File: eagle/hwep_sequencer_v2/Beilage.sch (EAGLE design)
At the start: 183 parts, among them X1 ESP32-AZDEL

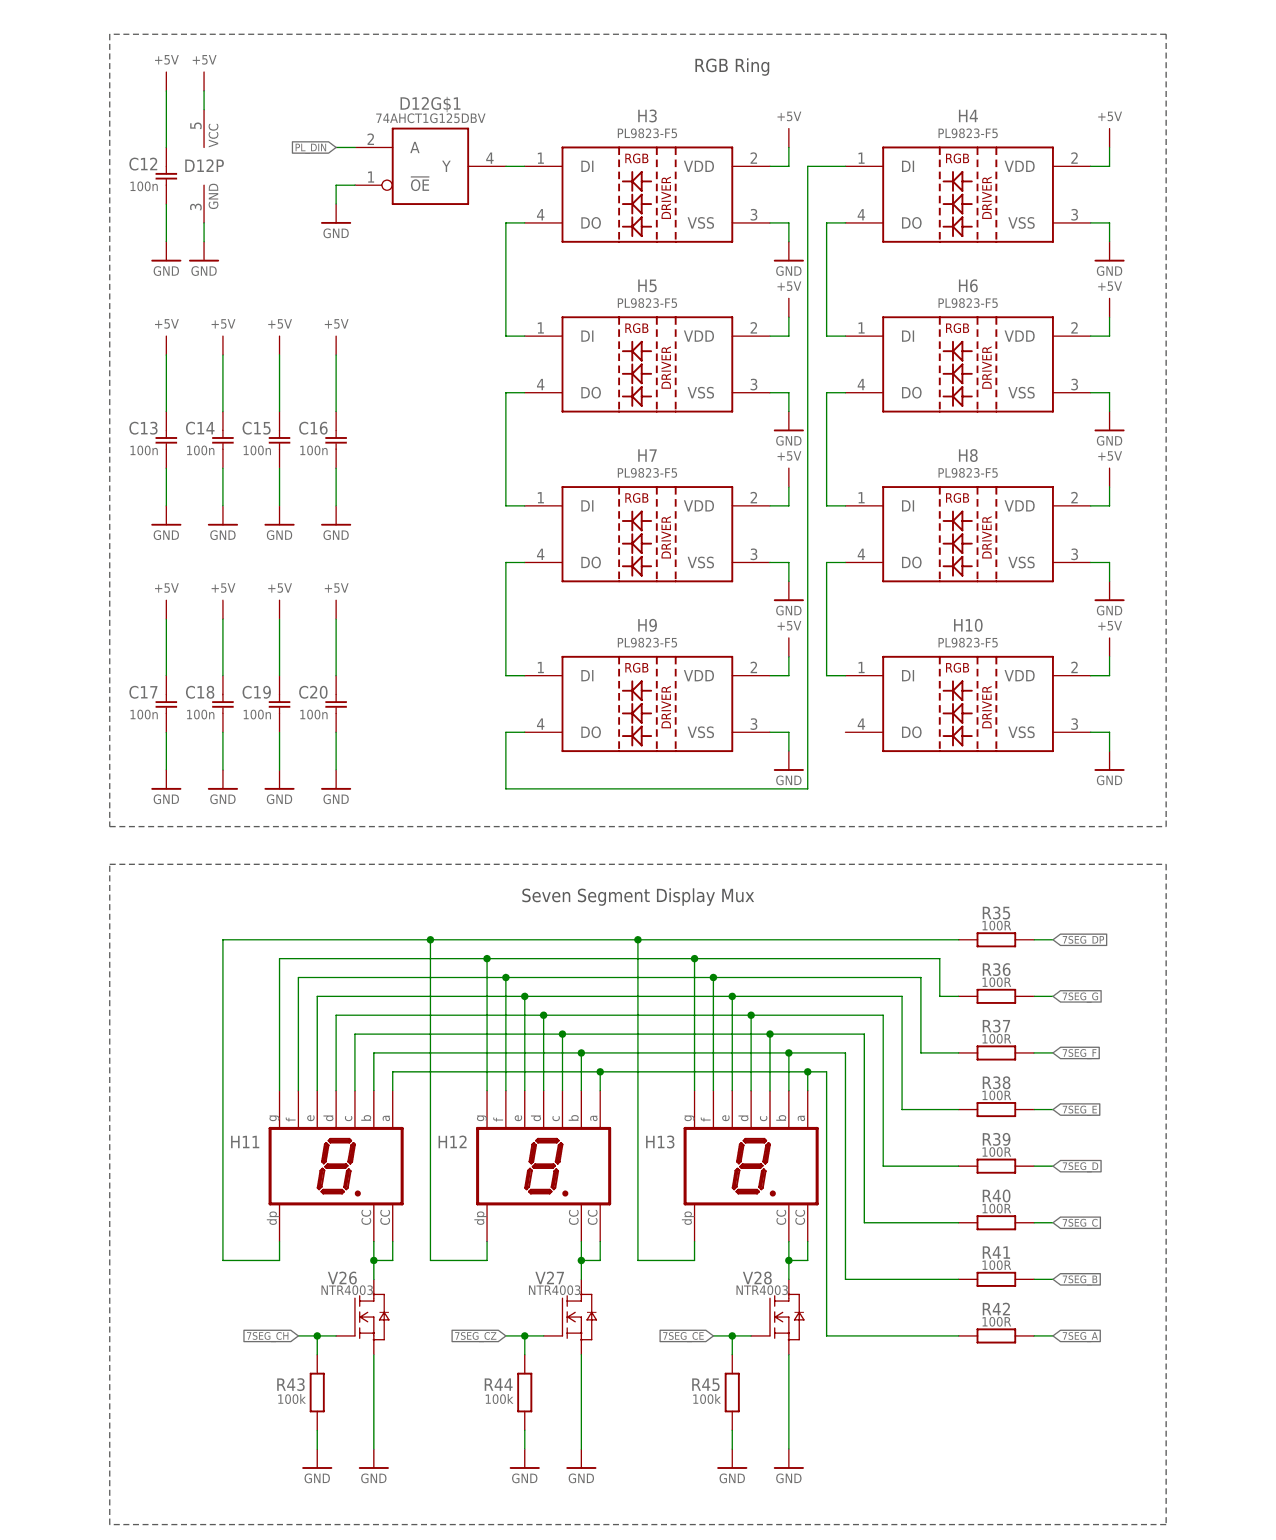
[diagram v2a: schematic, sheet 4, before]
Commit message: RGB Ring now in SMD
SMD RGB LEDS WS2812 used because of availability
PSU Buck Converter 12v to 5v still to be added to the schematic
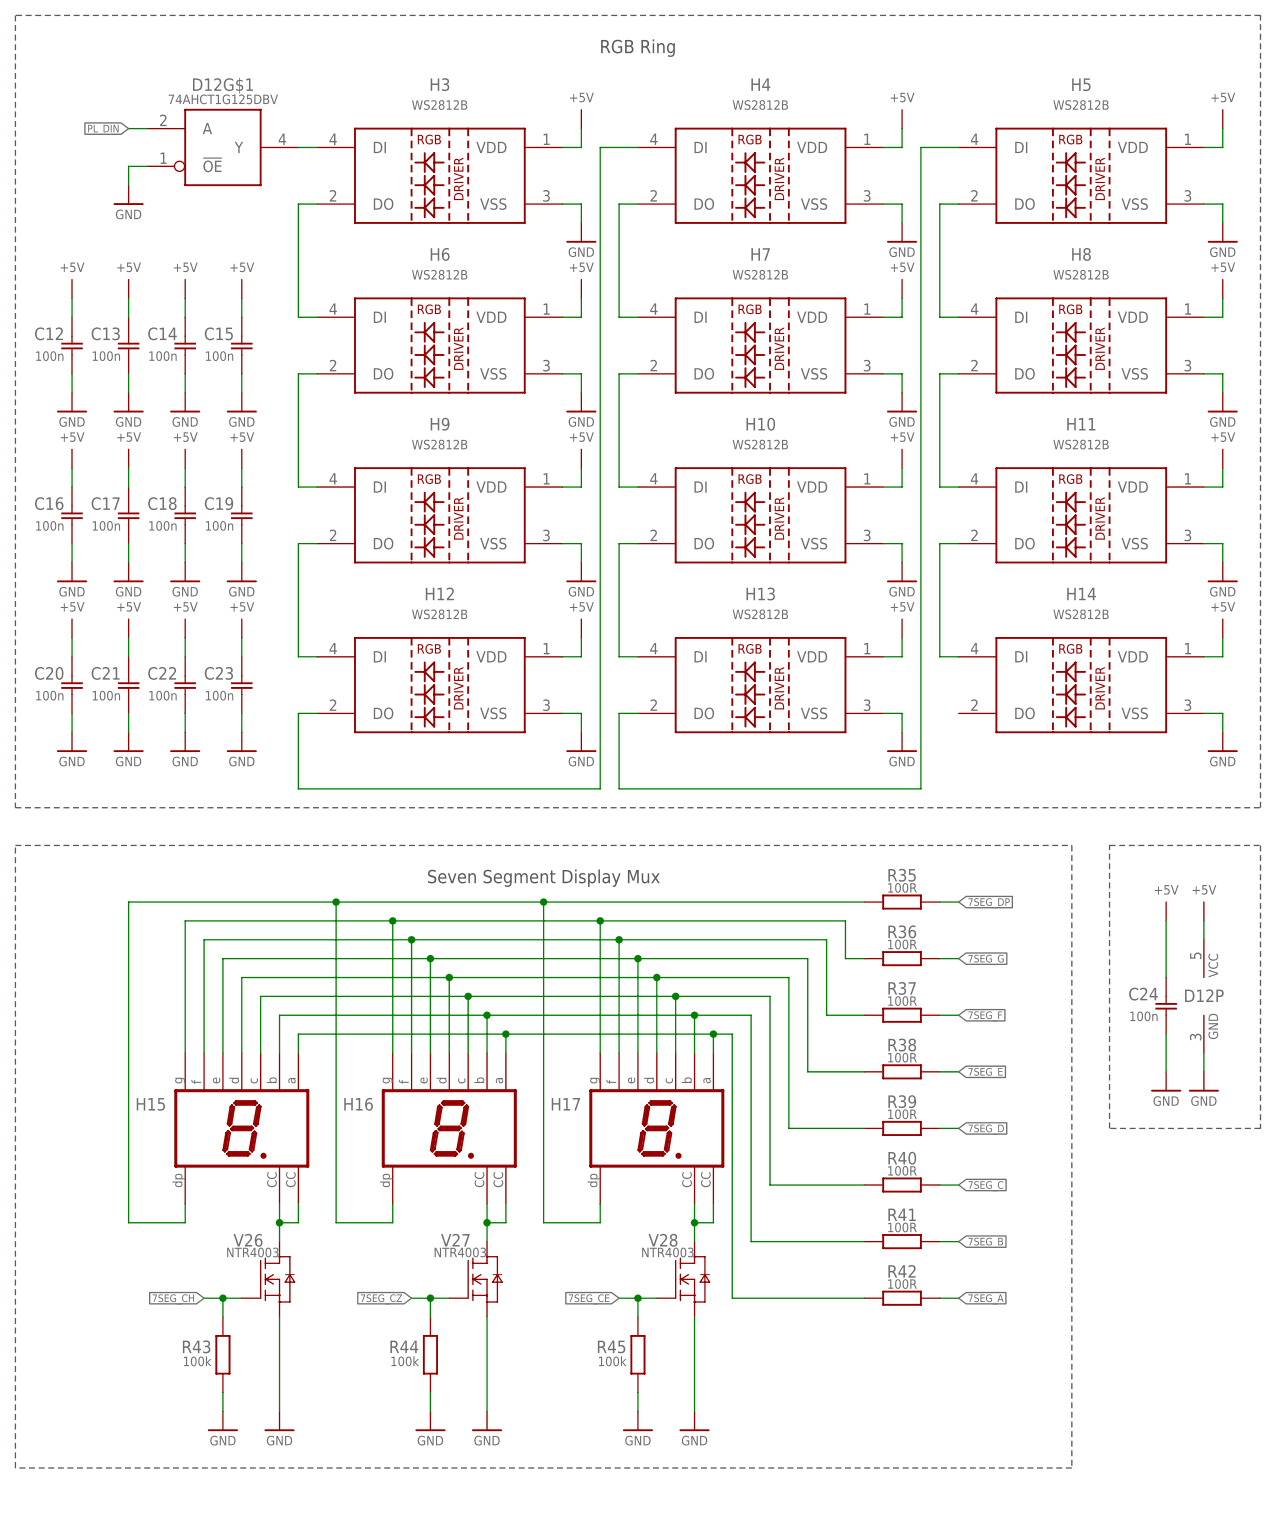
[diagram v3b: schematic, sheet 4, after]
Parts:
- added C29, C30: 1u, rcl_GruS:C-EUC0805
- added C31, C32: 100n, rcl_GruS:C-EUC0805
- added H46, H47, H48, H49: ge, led_GruS:LED5MM
- C21, C22: value 1u -> 100n
- H10, H3, H4, H5, H6, H7, H8, H9: value PL9823-F5 -> WS2812B; device led_GruS:PL9823-F5 -> led_GruS:WS2812B; CATEGORY 7 -> (none)
- H11, H12, H13: value (none) -> WS2812B; device display_GruS:HD-H103 -> led_GruS:WS2812B; CATEGORY 15 -> (none)
- H14: value rt -> WS2812B; device led_GruS:LEDCHIPLED_1206 -> led_GruS:WS2812B; CATEGORY 7 -> (none)
- H15, H16, H17: value rt -> (none); device led_GruS:LEDCHIPLED_1206 -> display_GruS:HD-H103; CATEGORY 7 -> 15
- H30, H31, H32, H33: value gn -> rt; device led_GruS:LED5MM -> led_GruS:LEDCHIPLED_1206
- H38, H39, H40, H41: value ge -> gn
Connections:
- new net N$67: H12.DO, H4.DI
- new net N$69: H5.DO, H8.DI
- new net N$71: H11.DI, H8.DO
- new net N$72: H11.DO, H14.DI
- net +3V3: now also C29.1, C30.1, C31.1, C32.1, H46.A, H47.A, H48.A, H49.A; no longer C21.1, C22.1, C23.1, C24.1, H14.A, H15.A, H16.A, H17.A
- net +5V: now also C21.1, C22.1, C23.1, C24.1, H11.VDD, H12.VDD, H13.VDD, H14.VDD
- net GND: now also C29.2, C30.2, C31.2, C32.2, H11.VSS, H12.VSS, H13.VSS, H14.VSS
- net N$10: now also H18.C; no longer H14.C
- net N$11: now also H19.C; no longer H15.C
- net N$12: now also H20.C; no longer H16.C
- net N$13: now also H21.C; no longer H17.C
- net N$20: now also H22.C; no longer H18.C
- net N$21: now also H23.C; no longer H19.C
- net N$22: now also H24.C; no longer H20.C
- net N$23: now also H25.C; no longer H21.C
- net N$25: now also H26.C; no longer H22.C
- net N$26: now also H27.C; no longer H23.C
- net N$27: now also H28.C; no longer H24.C
- net N$28: now also H29.C; no longer H25.C
- net N$29: now also H30.C; no longer H26.C
- net N$30: now also H31.C; no longer H27.C
- net N$31: now also H32.C; no longer H28.C
- net N$32: now also H33.C; no longer H29.C
- net N$33: now also H15.G, H16.G, H17.G; no longer H11.G, H12.G, H13.G
- net N$35: now also H15.F, H16.F, H17.F; no longer H11.F, H12.F, H13.F
- net N$36: now also H15.A, H16.A, H17.A; no longer H11.A, H12.A, H13.A
- net N$37: now also H15.B, H16.B, H17.B; no longer H11.B, H12.B, H13.B
- net N$38: now also H34.C; no longer H30.C
- net N$39: now also H35.C; no longer H31.C
- net N$4: now also H13.DO, H5.DI; no longer H4.DI, H9.DO
- net N$40: now also H36.C; no longer H32.C
- net N$41: now also H37.C; no longer H33.C
- net N$42: now also H38.C; no longer H34.C
- net N$43: now also H39.C; no longer H35.C
- net N$44: now also H40.C; no longer H36.C
- net N$45: now also H41.C; no longer H37.C
- net N$46: now also H42.C; no longer H38.C
- net N$47: now also H43.C; no longer H39.C
- net N$48: now also H44.C; no longer H40.C
- net N$49: now also H45.C; no longer H41.C
- net N$50: now also H46.C; no longer H42.C
- net N$51: now also H47.C; no longer H43.C
- net N$52: now also H48.C; no longer H44.C
- net N$53: now also H49.C; no longer H45.C
- net N$55: now also H15.CC, H15.CC@1; no longer H11.CC, H11.CC@1
- net N$56: now also H15.D, H16.D, H17.D; no longer H11.D, H12.D, H13.D
- net N$57: now also H7.DI; no longer H6.DI
- net N$59: now also H10.DI, H7.DO; no longer H6.DO, H8.DI
- net N$63: now also H10.DO, H13.DI; no longer H10.DI, H8.DO
- net N$64: now also H16.CC, H16.CC@1; no longer H12.CC, H12.CC@1
- net N$65: now also H17.CC, H17.CC@1; no longer H13.CC, H13.CC@1
- net N$68: now also H6.DI; no longer H5.DI
- net N$7: now also H15.DP, H16.DP, H17.DP; no longer H11.DP, H12.DP, H13.DP
- net N$70: now also H6.DO, H9.DI; no longer H5.DO, H7.DI
- net N$73: now also H12.DI, H9.DO; no longer H7.DO, H9.DI
- net N$78: now also H15.C, H16.C, H17.C; no longer H11.C, H12.C, H13.C
- net N$80: now also H15.E, H16.E, H17.E; no longer H11.E, H12.E, H13.E
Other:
- moved on the sheet: C12, C13, C14, C15, C16, C17, C18, C19, C20, C25, C26, C27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

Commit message: Major Prescaler Update
Optimized Prescaler:
Now Fully Software side.
Inputs are priority encoded and put on MCP23S08 free input pins.
Issues:
Analog Reference Voltage Needed?
Dedicated PSU / Voltage converter
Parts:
- removed C31, C32: 100n, rcl_GruS:C-EUC0805
- removed D14, D16: 74AHC1G04DBV, 74xx_GruS:74AHC1G04DBV
- removed D15: STP16CP05TTR, ic_GruS:STP16CP05TTR
- removed R14, R18: 56k, rcl_GruS:R-EUSR0805
- removed R2, R9: 10k, rcl_GruS:P160L
- removed R35, R36, R37, R38, R39, R40, R41, R42: 100R, rcl_GruS:R-EU_R0805
- removed R43, R44, R45: 100k, rcl_GruS:R-EUSR0805
- removed R46, R48: 10k, rcl_GruS:R-EUSR0805
- removed R47, R49: 2k7, rcl_GruS:R-EUSR0805
- removed V10, V11, V12, V13, V14, V15, V16, V17, V18, V19, V20, V21, V22, V23, V24, V25, V4, V5, V6, V7, V8, V9: 1N4148-7, diode_GruS:1N4148-7
- removed V26, V27, V28: NTR4003, mfet_GruS:NTR4003
- C10, C11, C25, C26, C29, C30: value 1u -> 100n
- C23, C24, C27, C28: value 100n -> 1u
- C4, C5: value 100n -> 10n
- C6, C7: value 10n -> 100n
- D1: value 74AHC138N -> MCP23S08SO; device 74xx_GruS:74AHC138N -> ic_GruS:MCP23S08SO
- D10: value 74HC73N -> STP16CP05TTR; device 74xx_GruS:74HC73N -> ic_GruS:STP16CP05TTR
- D11: value 74HC151N -> 74AHC1G04DBV; device 74xx_GruS:74HC151N -> 74xx_GruS:74AHC1G04DBV
- D12: value 74AHCT1G125DBV -> STP16CP05TTR; device 74xx_GruS:74AHCT1G125DBV -> ic_GruS:STP16CP05TTR
- D13: value STP16CP05TTR -> 74AHC1G04DBV; device ic_GruS:STP16CP05TTR -> 74xx_GruS:74AHC1G04DBV
- D2: value MCP23S08SO -> 74AHC1G125DBV; device ic_GruS:MCP23S08SO -> 74xx_GruS:74AHC1G125DBV
- D4: value 74AHC1G125DBV -> 74AHC138N; device 74xx_GruS:74AHC1G125DBV -> 74xx_GruS:74AHC138N
- D6: value 74HC151N -> 74HC148N; device 74xx_GruS:74HC151N -> 74xx_GruS:74HC148N; CATEGORY 13 -> (none)
- D7: value 74HC193D -> 74HC148N; device 74xx_GruS:74HC193D -> 74xx_GruS:74HC148N; CATEGORY 13 -> (none)
- D8: value 74HC73N -> 74HC00N; device 74xx_GruS:74HC73N -> 74xx_GruS:74HC00N; CATEGORY 13 -> (none)
- D9: value 74HC73N -> 74AHCT1G125DBV; device 74xx_GruS:74HC73N -> 74xx_GruS:74AHCT1G125DBV
- R13: value 56k -> 10k; device rcl_GruS:R-EUSR0805 -> rcl_GruS:P160L
- R15, R16, R17, R19: value 56k -> 10k
- R20: value 10k -> 100R; device rcl_GruS:R-EUSR0805 -> rcl_GruS:R-EU_R0805
- R21: value 100k -> 100R; device rcl_GruS:R-EUSR0805 -> rcl_GruS:R-EU_R0805
- R22, R23, R24, R25, R26, R27: value 100k -> 100R
- R29, R30: device rcl_GruS:R-EU_R0805 -> rcl_GruS:R-EUSR0805
- R31, R33: value 100k -> 10k; device rcl_GruS:R-EU_R0805 -> rcl_GruS:R-EUSR0805
- R32, R34: value 100k -> 2k7; device rcl_GruS:R-EU_R0805 -> rcl_GruS:R-EUSR0805
- R6: value 330R -> 10k; device rcl_GruS:R-EUSR0805 -> rcl_GruS:P160L
- R7: value 330R -> 1k
- R8: value 1M -> 1k
- S14: value (none) -> EC11E09244AQ; device switch_GruS:TASTE10XX -> switch_GruS:EC11E09244AQ
- S15: value EC11E09244AQ -> (none); device switch_GruS:EC11E09244AQ -> switch_GruS:TASTE10XX
- V2, V3: value 1N4148-7 -> NTR4003; device diode_GruS:1N4148-7 -> mfet_GruS:NTR4003
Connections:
- removed net !CS!_C: D1.C, X1.GPIO22
- removed net BPM_DIV_Q0: D6.A, D9B.Q
- removed net BPM_DIV_Q1: D10A.Q, D6.B
- removed net BPM_DIV_Q2: D10B.Q, D6.C
- removed net GATE_DIV_Q0: D11.A, D8B.Q
- removed net GATE_DIV_Q1: D11.B, D8A.Q
- removed net GATE_DIV_Q2: D11.C, D9A.Q
- removed net N$14: D8A.K, R25.2, V6.C, V9.C
- removed net N$15: D9B.K, R30.2, V14.C, V16.C
- removed net N$16: D10B.K, R34.2, V23.C, V24.C, V25.C
- removed net N$17: D10B.J, R33.2, V22.C
- removed net N$18: D10A.J, R31.2, V19.C, V20.C
- removed net N$19: D9B.J, R29.2, V15.C, V17.C
- removed net N$2: D8B.K, R23.2, V2.C, V4.C
- removed net N$3: D8A.J, R24.2, V7.C, V8.C
- removed net N$34: D10A.K, R32.2, V18.C, V21.C
- removed net N$5: D8B.J, R22.2, V3.C, V5.C
- removed net N$6: D9A.K, R27.2, V11.C, V12.C, V13.C
- removed net N$60: R6.1, V1.D
- removed net PS_BPM: D6.Y, X1.GPIO35/ADC1_CH7
- removed net PS_GATE: D11.Y, X1.GPIO34/ADC1_CH6
- removed net Q0: D11.D1, D6.D1, D7G$1.Q0
- removed net Q1: D11.D2, D6.D2, D7G$1.Q1
- removed net Q2: D11.D3, D6.D3, D7G$1.Q2
- removed net Q3: D11.D4, D6.D4, D7G$1.Q3
- removed net SRC_BPM: D10A.!CLK, D10B.!CLK, D11.D0, D6.D0, D7G$1.CPD, D8A.!CLK, D8B.!CLK, D9A.!CLK, D9B.!CLK, X1.GPIO32/ADC1_CH4
- new net AGND: C6.2, D5.AGND, R10.1, R11.1, R12.1, R13.1, R3.1, R4.1, R5.1, R6.1
- new net GS_B: D6.GS, D8D.A
- new net GS_G: D7.GS, D8D.B
- new net PS0: D1.GP4, D8A.Y
- new net PS1: D1.GP5, D8B.Y
- new net PS2: D1.GP6, D8C.Y
- new net PS3: D1.GP7, D8D.Y
- new net PS_B0: D6.A0, D8A.A
- new net PS_B1: D6.A1, D8B.A
- new net PS_B2: D6.A2, D8C.A
- new net PS_G0: D7.A0, D8A.B
- new net PS_G1: D7.A1, D8B.B
- new net PS_G2: D7.A2, D8C.B
- net !CS!_A: now also D4.A; no longer D1.A
- net !CS!_B: now also D4.B; no longer D1.B
- net +3V3: now also C23.1, C24.1, C6.1, C7.1, D1.!RESET, D1.VDD, D10.VDD, D11G$2.VCC, D12.VDD, D13G$2.VCC, D2P.VCC, D4.G1, D4.VCC, D6.0, D6.1, D6.2, D7.0, D7.1, D7.2, D7.VCC, D8P.VCC, R13.2, R15.2, R16.2, R31.2, R33.2, R6.2, S14.WIPER; no longer C10.1, C11.1, C31.1, C32.1, C4.1, C5.1, D1.G1, D1.VCC, D10/P.VCC, D11.VCC, D13.VDD, D14G$2.VCC, D15.VDD, D16G$2.VCC, D2.!RESET, D2.VDD, D4P.VCC, D7/P.VCC, D7G$1.!PL, D7G$1.CPU, D8/P.VCC, D9/P.VCC, H1.A, R18.2, R2.2, R20.2, R21.2, R28.2, R46.2, R48.2, R9.2, S10.P1, S11.P, S12.P, S13.P1, S14.P, S2.P, S3.P, S4.P, S5.P, S7.P1, S8.P1, S9.P1
- net +5V: now also C10.1, C11.1, D9P.VCC; no longer C23.1, C24.1, D12P.VCC
- net 088S052_!CS!: now also D4.Y3, R19.1; no longer D1.Y3, R20.1
- net 23S08_!CS: now also D1.!CS, D2G$1.!OE, D4.Y0; no longer D1.Y0, D2.!CS, D4G$1.!OE
- net 7SEG_A: now also R27.2; no longer R42.2
- net 7SEG_B: now also R26.2; no longer R41.2
- net 7SEG_C: now also R25.2; no longer R40.2
- net 7SEG_CE: now also R30.2, V3.G; no longer R45.2, V28.G
- net 7SEG_CH: now also R28.2, V1.G; no longer R43.2, V26.G
- net 7SEG_CZ: now also R29.2, V2.G; no longer R44.2, V27.G
- net 7SEG_D: now also R24.2; no longer R39.2
- net 7SEG_DP: now also R20.2; no longer R35.2
- net 7SEG_E: now also R23.2; no longer R38.2
- net 7SEG_F: now also R22.2; no longer R37.2
- net 7SEG_G: now also R21.2; no longer R36.2
- net ADC0: now also R3.3; no longer R2.3
- net ADC1: now also R4.3; no longer R3.3
- net ADC2: now also R5.3; no longer R4.3
- net ADC3: now also R6.3; no longer R5.3
- net ADC4: now also R10.3; no longer R9.3
- net ADC5: now also R11.3; no longer R10.3
- net ADC6: now also R12.3; no longer R11.3
- net ADC7: now also R13.3; no longer R12.3
- net CLRR: now also D1.GP1; no longer D2.GP1, R16.2
- net EC11_A: now also C4.1, R15.1, S14.CW; no longer C6.1, R17.1, S15.CW
- net EC11_B: now also C5.1, R16.1, S14.CCW; no longer C7.1, R18.1, S15.CCW
- net EC11_SW: now also R17.1, S14.NO; no longer R19.1, S15.NO
- net EVENT: now also D1.GP0, H1.A, S12.S1; no longer D2.GP0, R15.2, R8.2, S13.S1, V1.G
- net GND: now also D1.A0, D1.A1, D1.VSS, D10.!OE!/!DM2, D10.GND, D11G$2.GND, D12.!OE!/!DM2, D12.GND, D13G$2.GND, D2P.GND, D4.!G2A, D4.!G2B, D4.GND, D6.EI, D7.GND, D8P.GND, D9G$1.!OE, D9P.GND, R28.1, S1.P1, S10.P, S10.P1, S11.P, S11.P1, S12.P, S12.P1, S13.P, S13.P1, S14.COM, S14.MH1, S14.MH2, S15.P, S15.P1, S2.P, S2.P1, S3.P, S3.P1, S4.P, S4.P1, S5.P, S5.P1, S6.P1, S7.P, S7.P1, S8.P, S8.P1, S9.P, S9.P1, V2.S, V3.S; no longer C31.2, C32.2, C6.2, D1.!G2A, D1.!G2B, D1.GND, D10/P.GND, D11.!G, D11.GND, D12G$1.!OE, D12P.GND, D13.!OE!/!DM2, D13.GND, D14G$2.GND, D15.!OE!/!DM2, D15.GND, D16G$2.GND, D2.A0, D2.A1, D2.VSS, D4P.GND, D5.AGND, D6.!G, D7/P.GND, D7G$1.MR, D8/P.GND, D9/P.GND, R10.1, R11.1, R12.1, R13.1, R14.1, R15.1, R16.1, R2.1, R22.1, R23.1, R24.1, R25.1, R26.1, R27.1, R3.1, R31.1, R33.1, R4.1, R43.1, R44.1, R45.1, R47.1, R49.1, R5.1, R9.1, S15.COM, S15.MH1, S15.MH2, S15.WIPER, V26.S, V27.S, V28.S
- net MISO: now also D2G$1.Y; no longer D4G$1.Y
- net MOSI: now also D10.SDI, D12.SDI; no longer D13.SDI, D15.SDI
- net N$1: now also D6.EO, D7.EI; no longer D9A.J, R26.2, V10.C
- net N$10: now also D10.!OUT0; no longer D13.!OUT0
- net N$11: now also D10.!OUT1; no longer D13.!OUT1
- net N$12: now also D10.!OUT2; no longer D13.!OUT2
- net N$13: now also D10.!OUT3; no longer D13.!OUT3
- net N$20: now also D10.!OUT4; no longer D13.!OUT4
- net N$21: now also D10.!OUT5; no longer D13.!OUT5
- net N$22: now also D10.!OUT6; no longer D13.!OUT6
- net N$23: now also D10.!OUT7; no longer D13.!OUT7
- net N$24: now also D10.R-EXT, R32.2; no longer D13.R-EXT, R47.2
- net N$25: now also D10.!OUT8; no longer D13.!OUT8
- net N$26: now also D10.!OUT9; no longer D13.!OUT9
- net N$27: now also D10.!OUT10; no longer D13.!OUT10
- net N$28: now also D10.!OUT11; no longer D13.!OUT11
- net N$29: now also D10.!OUT12; no longer D13.!OUT12
- net N$30: now also D10.!OUT13; no longer D13.!OUT13
- net N$31: now also D10.!OUT14; no longer D13.!OUT14
- net N$32: now also D10.!OUT15; no longer D13.!OUT15
- net N$33: now also R21.1; no longer R36.1
- net N$35: now also R22.1; no longer R37.1
- net N$36: now also R27.1; no longer R42.1
- net N$37: now also R26.1; no longer R41.1
- net N$38: now also D12.!OUT0; no longer D15.!OUT0
- net N$39: now also D12.!OUT1; no longer D15.!OUT1
- net N$40: now also D12.!OUT2; no longer D15.!OUT2
- net N$41: now also D12.!OUT3; no longer D15.!OUT3
- net N$42: now also D12.!OUT4; no longer D15.!OUT4
- net N$43: now also D12.!OUT5; no longer D15.!OUT5
- net N$44: now also D12.!OUT6; no longer D15.!OUT6
- net N$45: now also D12.!OUT7; no longer D15.!OUT7
- net N$46: now also D12.!OUT8; no longer D15.!OUT8
- net N$47: now also D12.!OUT9; no longer D15.!OUT9
- net N$48: now also D12.!OUT10; no longer D15.!OUT10
- net N$49: now also D12.!OUT11; no longer D15.!OUT11
- net N$50: now also D12.!OUT12; no longer D15.!OUT12
- net N$51: now also D12.!OUT13; no longer D15.!OUT13
- net N$52: now also D12.!OUT14; no longer D15.!OUT14
- net N$53: now also D12.!OUT15; no longer D15.!OUT15
- net N$54: now also D12.R-EXT, R34.2; no longer D15.R-EXT, R49.2
- net N$55: now also V1.D; no longer V26.D
- net N$56: now also R24.1; no longer R39.1
- net N$58: now also R7.2; no longer R6.2
- net N$61: now also D12.LE/DM1, D13G$1.Y, R33.1; no longer D15.LE/DM1, D16G$1.Y, R48.1
- net N$62: now also D1.SO, D2G$1.A; no longer D2.SO, D4G$1.A
- net N$64: now also V2.D; no longer V27.D
- net N$65: now also V3.D; no longer V28.D
- net N$66: now also D10.LE/DM1, D11G$1.Y, R31.1; no longer D13.LE/DM1, D14G$1.Y, R46.1
- net N$7: now also R20.1; no longer R35.1
- net N$78: now also R25.1; no longer R40.1
- net N$8: now also D9G$1.Y; no longer D12G$1.Y
- net N$80: now also R23.1; no longer R38.1
- net N$9: now also R8.2; no longer R7.2
- net PAUSE_CNT: now also D1.GP3, S13.S1; no longer D2.GP3, R13.2, S12.S
- net PL_DIN: now also D9G$1.A; no longer D12G$1.A
- net Q0_SW_BD: now also D6.6, S2.S1; no longer S2.S, V17.A, V21.A, V25.A
- net Q0_SW_GD: now also D7.6; no longer V13.A, V5.A, V9.A
- net Q1_SW_BD: now also D6.5, S3.S1; no longer S3.S, V16.A, V20.A, V24.A
- net Q1_SW_GD: now also D7.5; no longer V12.A, V4.A, V8.A
- net Q2_SW_BD: now also D6.4; no longer V15.A, V19.A, V23.A
- net Q2_SW_GD: now also D7.4, S9.S; no longer S9.S1, V11.A, V3.A, V7.A
- net Q3_SW_BD: now also D6.3, S5.S1; no longer S5.S, V14.A, V18.A, V22.A
- net Q3_SW_GD: now also D7.3; no longer V10.A, V2.A, V6.A
- net RESET_CNT: now also D1.GP2, S15.S; no longer D2.GP2, R14.2, S14.S
- net SCK: now also D1.SCK, D10.CLK, D12.CLK; no longer D13.CLK, D15.CLK, D2.SCK
- net SRC_SW_BD: now also D6.7, S1.S1; no longer D10A.!CLR, D10B.!CLR, D9B.!CLR, R28.1, S1.S
- net SRC_SW_GD: now also D7.7, S6.S1; no longer D8A.!CLR, D8B.!CLR, D9A.!CLR, R21.1, S6.S
- net STP_LE_K: now also D11G$1.A, D4.Y2; no longer D1.Y2, D14G$1.A
- net STP_LE_S: now also D13G$1.A, D4.Y1; no longer D1.Y1, D16G$1.A
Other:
- note added: "-?- Eigene Referenzspannung für Analog -?- Spannungsversorgung"
- note added: "Input ADC"
- note added: "Internal Weak Pullup"
- note added: "Prescaler 4-bit encoded data priority on BPM Divider Inputs"
- note added: "Prescaler Input Encoder"
- note removed: "Gate- & BPM-Prescaler"
- note removed: "Power Pins"
- note removed: "Pull Resistors"
- note removed: "Switch Matrix for Prescaler Settings"
